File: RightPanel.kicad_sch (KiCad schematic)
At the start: 20 parts, among them U1 74LS596, U2 74LS596, U25 TPS54302

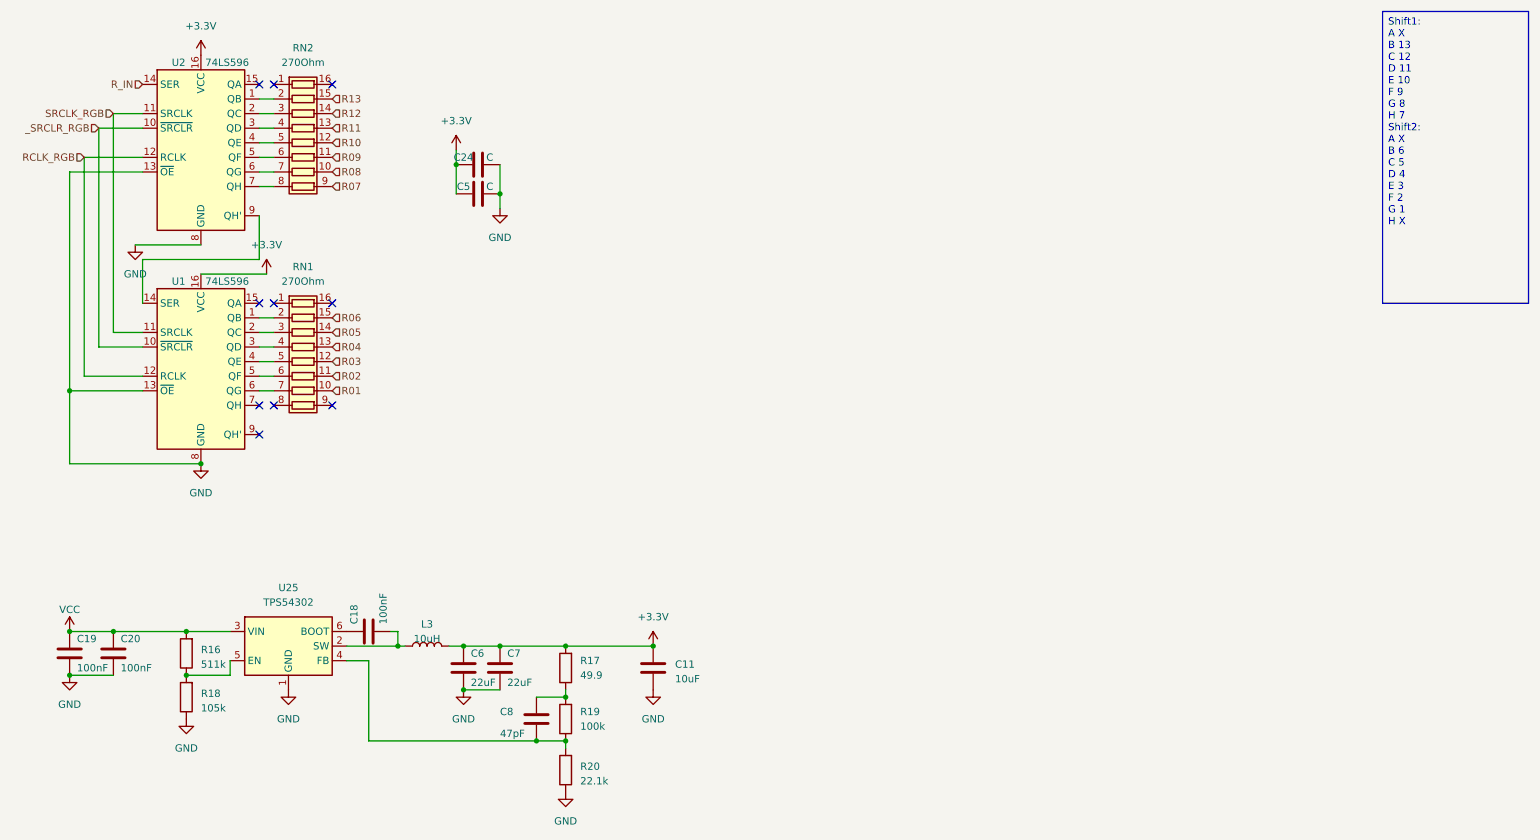
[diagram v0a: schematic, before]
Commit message: update
break down schemantic to panels, added controller and additional commponents, fixed
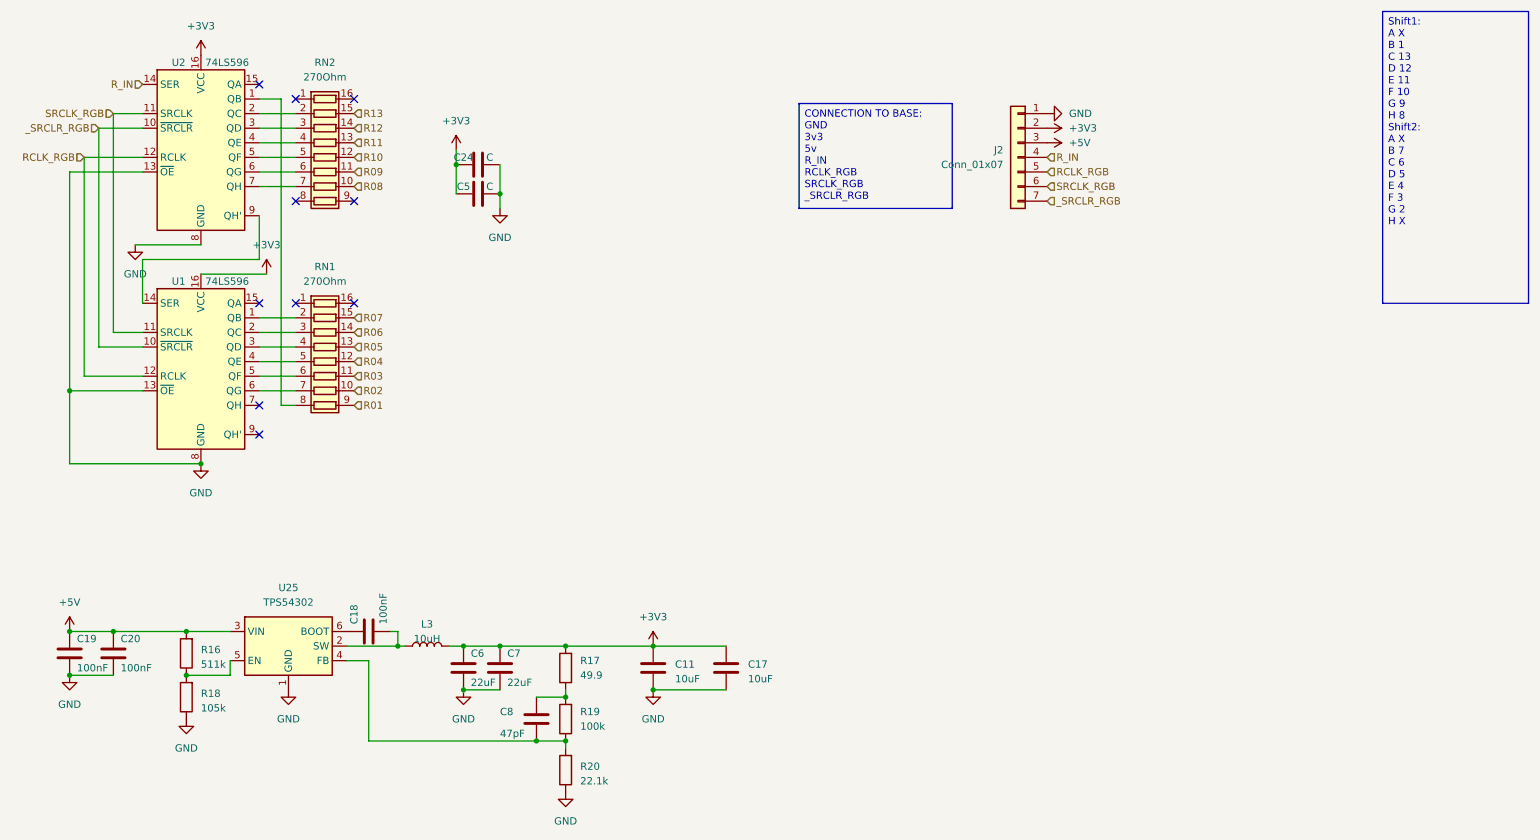
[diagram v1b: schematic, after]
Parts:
- added C17: 10uF, Capacitor_SMD:C_1206_3216Metric_Pad1.33x1.80mm_HandSolder, symbol Device:C
- added J2: Conn_01x07, Connector_PinSocket_2.54mm:PinSocket_1x07_P2.54mm_Vertical, symbol Connector_Generic:Conn_01x07
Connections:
- net GND: now also C17.2, J2.1 (Pin_1)
- net R01: now also RN1.9 (R8.2); no longer RN1.10 (R7.2)
- net R02: now also RN1.10 (R7.2); no longer RN1.11 (R6.2)
- net R03: now also RN1.11 (R6.2); no longer RN1.12 (R5.2)
- net R04: now also RN1.12 (R5.2); no longer RN1.13 (R4.2)
- net R05: now also RN1.13 (R4.2); no longer RN1.14 (R3.2)
- net R06: now also RN1.14 (R3.2); no longer RN1.15 (R2.2)
- net R07: now also RN1.15 (R2.2); no longer RN2.9 (R8.2)
- net RCLK_RGB: now also J2.5 (Pin_5)
- net R_IN: now also J2.4 (Pin_4)
- net SRCLK_RGB: now also J2.6 (Pin_6)
- net _SRCLR_RGB: now also J2.7 (Pin_7)
- net at RN1.8 (R8.1): now also U2.1 (QB)
- net at RN2.2 (R2.1): now also U2.2 (QC); no longer U2.1 (QB)
- net at RN2.3 (R3.1): now also U2.3 (QD); no longer U2.2 (QC)
- net at RN2.4 (R4.1): now also U2.4 (QE); no longer U2.3 (QD)
- net at RN2.5 (R5.1): now also U2.5 (QF); no longer U2.4 (QE)
- net at RN2.6 (R6.1): now also U2.6 (QG); no longer U2.5 (QF)
- net at RN2.7 (R7.1): now also U2.7 (QH); no longer U2.6 (QG)
- net at RN2.8 (R8.1): no longer U2.7 (QH)
- net +3.3V renamed +3V3
- net +3V3: now also C17.1, J2.2 (Pin_2)
- net VCC renamed +5V
- net +5V: now also J2.3 (Pin_3)
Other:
- moved on the sheet: RN2
